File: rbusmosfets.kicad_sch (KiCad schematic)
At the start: 26 parts, among them J1 RBUS, J4 Conn_01x02_Male, Q4 PXP012-30QLJ, Q5 PXP012-30QLJ, Q6 PXP012-30QLJ, Q7 PXP012-30QLJ, U10 LTC4412xS6, U5 74AHC1G00, U6 74AHC1G08, U9 LTC4412xS6

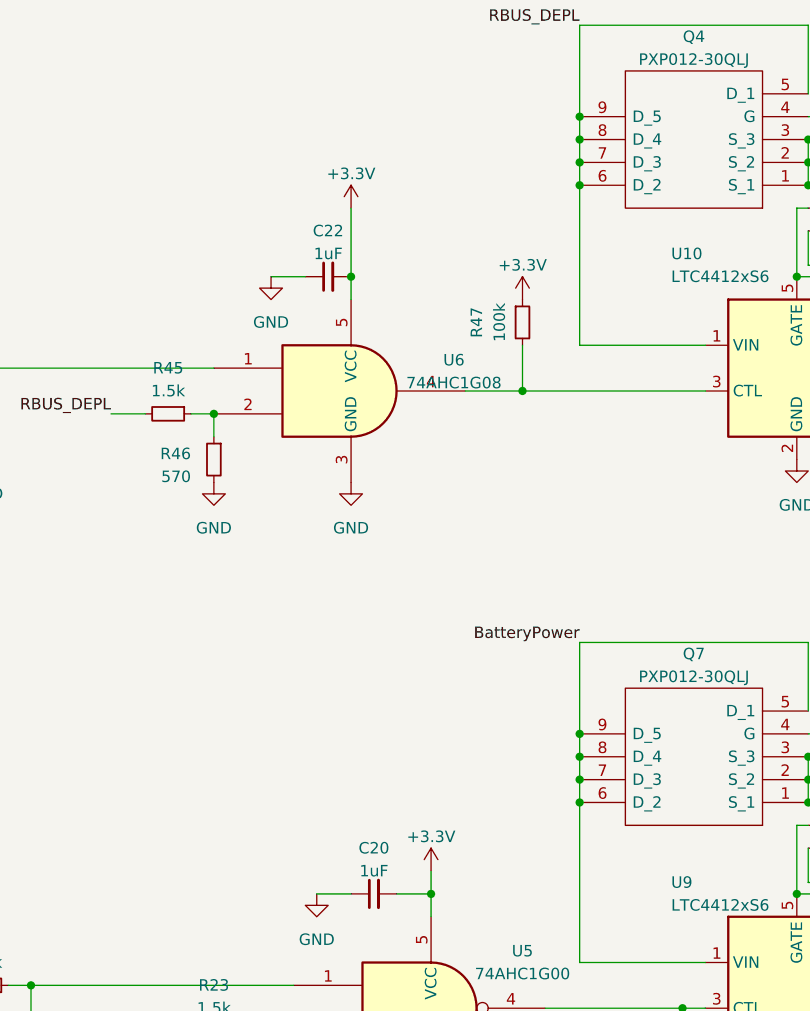
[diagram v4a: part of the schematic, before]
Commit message: almost all drc fixed (65 left)
- J2 hole intersects with pads? USB
- 3.3 regulator courtyard self intersecting?
- courtyard overlaps (does this matter?)
- padstack not valid? this is testpoints on the back with traces on the back, why is this bad?
- expected SMD actual through hole?
- front solder mask bridges items ?? testpoitns are on back layer
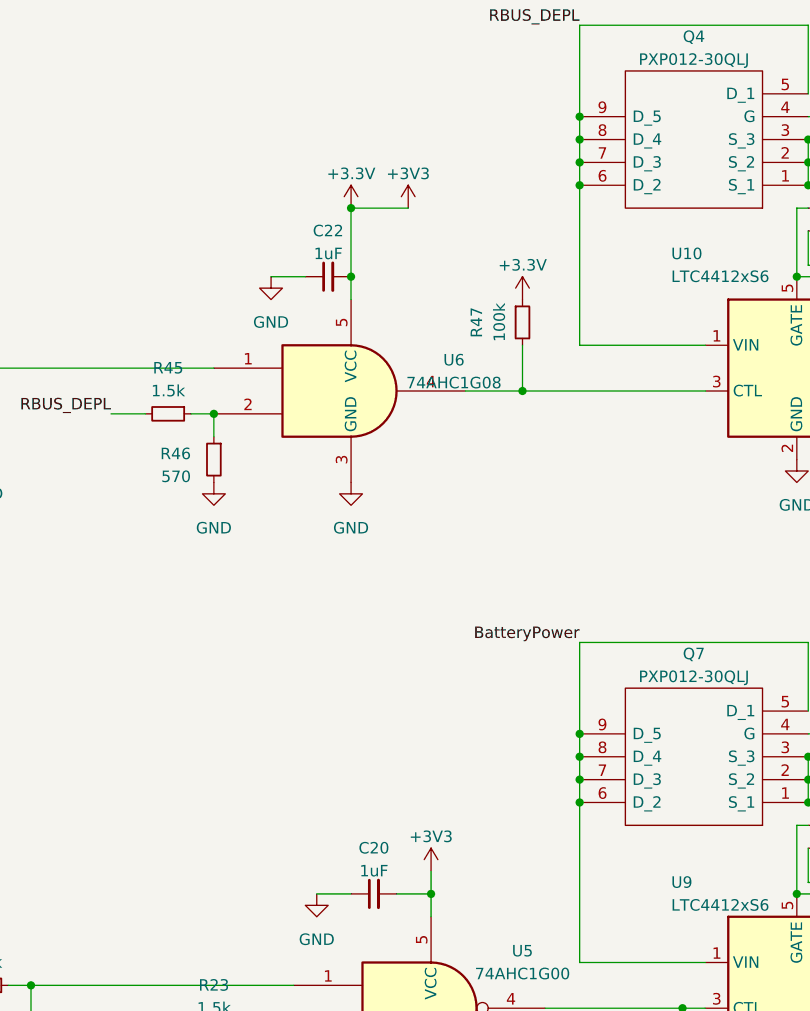
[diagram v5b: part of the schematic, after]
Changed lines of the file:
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@@
   (junction (at 212.09 107.95) (diameter 0) (color 0 0 0 0)
+  )
+  (junction (at 186.69 46.99) (diameter 0) (color 0 0 0 0)
   )
   (junction (at 212.09 110.49) (diameter 0) (color 0 0 0 0)
@@
   )
   (wire (pts (xy 135.89 64.77) (xy 138.43 64.77))
+    (stroke (width 0) (type default))
+  )
+  (wire (pts (xy 186.69 46.99) (xy 193.04 46.99))
     (stroke (width 0) (type default))
   )
@@
     )
   )
+  (symbol (lib_id "power:+3V3") (at 195.58 120.65 0) (unit 1)
+    (in_bom yes) (on_board yes) (dnp no) (fields_autoplaced)
+    (property "Reference" "#PWR083" (at 195.58 124.46 0)
+      (effects (font (size 1.27 1.27)) hide)
+    )
+    (property "Value" "+3V3" (at 195.58 116.84 0)
+      (effects (font (size 1.27 1.27)))
+    )
+    (property "Footprint" "" (at 195.58 120.65 0)
+      (effects (font (size 1.27 1.27)) hide)
+    )
+    (property "Datasheet" "" (at 195.58 120.65 0)
+      (effects (font (size 1.27 1.27)) hide)
+    )
+    (pin "1")
+    (instances
+      (project "Canardboard"
+        (path "/7db990e4-92e1-4f99-b4d2-435bbec1ba83/972bc3cd-df5c-4105-af8a-a8e2a9c5e16b"
+          (reference "#PWR083") (unit 1)
+        )
+      )
+    )
+  )
   (symbol (lib_id "power:VBUS") (at 48.26 59.69 0) (unit 1)
     (in_bom yes) (on_board yes) (dnp no) (fields_autoplaced)
@@
     )
   )
+  (symbol (lib_id "power:+3V3") (at 193.04 46.99 0) (mirror y) (unit 1)
+    (in_bom yes) (on_board yes) (dnp no)
+    (property "Reference" "#PWR051" (at 193.04 50.8 0)
+      (effects (font (size 1.27 1.27)) hide)
+    )
+    (property "Value" "+3V3" (at 193.04 43.18 0)
+      (effects (font (size 1.27 1.27)))
+    )
+    (property "Footprint" "" (at 193.04 46.99 0)
+      (effects (font (size 1.27 1.27)) hide)
+    )
+    (property "Datasheet" "" (at 193.04 46.99 0)
+      (effects (font (size 1.27 1.27)) hide)
+    )
+    (pin "1")
+    (instances
+      (project "Canardboard"
+        (path "/7db990e4-92e1-4f99-b4d2-435bbec1ba83/972bc3cd-df5c-4105-af8a-a8e2a9c5e16b"
+          (reference "#PWR051") (unit 1)
+        )
+      )
+    )
+  )
   (symbol (lib_name "GND_2") (lib_id "power:GND") (at 177.8 54.61 0) (unit 1)
     (in_bom yes) (on_board yes) (dnp no) (fields_autoplaced)
@@
         )
       )
-    )
-  )
-  (symbol (lib_id "power:+3.3V") (at 195.58 120.65 0) (unit 1)
-    (in_bom yes) (on_board yes) (dnp no) (fields_autoplaced)
-    (property "Reference" "#PWR051" (at 195.58 124.46 0)
-      (effects (font (size 1.27 1.27)) hide)
-    )
-    (property "Value" "+3.3V" (at 195.58 116.84 0)
-      (effects (font (size 1.27 1.27)))
-    )
-    (property "Footprint" "" (at 195.58 120.65 0)
-      (effects (font (size 1.27 1.27)) hide)
-    )
-    (property "Datasheet" "" (at 195.58 120.65 0)
-      (effects (font (size 1.27 1.27)) hide)
-    )
-    (pin "1")
-    (instances
-      (project "Canardboard"
-        (path "/7db990e4-92e1-4f99-b4d2-435bbec1ba83/972bc3cd-df5c-4105-af8a-a8e2a9c5e16b"
-          (reference "#PWR051") (unit 1)
-        )
-      )

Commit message: fixed all of andrei's comments v1
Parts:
- removed JP3: SolderJumper_2_Open, Jumper:SolderJumper-2_P1.3mm_Open_RoundedPad1.0x1.5mm, symbol Jumper:SolderJumper_2_Open
- added R48: 100k, Resistor_SMD:R_0402_1005Metric, symbol Device:R_Small
- added R8: 0, Resistor_SMD:R_0402_1005Metric, symbol Device:R_Small
- R15, R42, R44, R46: value 570 -> 470
- R16, R23, R43, R45: value 1.5k -> 1k
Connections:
- net +3.3V: now also R48.1
- net GND: now also R8.2
- net at U5.4, U9.3 (CTL): now also R48.2, R8.1
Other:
- moved on the sheet: C20, R15, R16, R23, R42, U5

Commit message: did some stuffus
added a new power plane in servo power on the back side
made SW larger
and a lot more changes
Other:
- note added: "This is a solder jumper"
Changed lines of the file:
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@@
     (stroke (width 0) (type default))
+  )
+  (text "This is a solder jumper\n" (at 193.04 139.7 0)
+    (effects (font (size 1.27 1.27)) (justify left bottom))
   )
   (label "RBUS_3.3" (at 138.43 173.99 90) (fields_autoplaced)

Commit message: new board just dropped
i hate my life
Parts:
- J4: footprint iclr:AMASS_XT60PW-F -> Connector_AMASS:AMASS_XT30PW-M_1x02_P2.50mm_Horizontal
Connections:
- net BatteryPower: now also J4.2 (Pin_2); no longer J4.1 (Pin_1)
- net GND: now also J4.1 (Pin_1); no longer J4.2 (Pin_2)
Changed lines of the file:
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@@
+    (stroke (width 0) (type default))
+  )
+  (wire (pts (xy 93.98 173.99) (xy 107.95 173.99))
     (stroke (width 0) (type default))
   )
@@
     (stroke (width 0) (type default))
   )
-  (wire (pts (xy 107.95 173.99) (xy 93.98 173.99))
-    (stroke (width 0) (type default))
-  )
   (wire (pts (xy 240.03 26.67) (xy 240.03 36.83))
     (stroke (width 0) (type default))
@@
     (stroke (width 0) (type default))
   )
+  (wire (pts (xy 123.19 171.45) (xy 93.98 171.45))
+    (stroke (width 0) (type default))
+  )
   (wire (pts (xy 163.83 69.85) (xy 160.02 69.85))
     (stroke (width 0) (type default))
@@
   )
   (wire (pts (xy 146.05 64.77) (xy 171.45 64.77))
-    (stroke (width 0) (type default))
-  )
-  (wire (pts (xy 107.95 171.45) (xy 93.98 171.45))
     (stroke (width 0) (type default))
   )
@@
     (effects (font (size 1.27 1.27)) (justify right bottom))
   )
-  (label "BatteryPower" (at 107.95 171.45 0) (fields_autoplaced)
+  (label "BatteryPower" (at 107.95 173.99 0) (fields_autoplaced)
     (effects (font (size 1.27 1.27)) (justify left bottom))
   )
@@
     )
   )
-  (symbol (lib_id "power:GND") (at 107.95 173.99 0) (unit 1)
-    (in_bom yes) (on_board yes) (dnp no)
-    (property "Reference" "#PWR065" (at 107.95 180.34 0)
-      (effects (font (size 1.27 1.27)) hide)
-    )
-    (property "Value" "GND" (at 107.95 179.07 0)
-      (effects (font (size 1.27 1.27)))
-    )
-    (property "Footprint" "" (at 107.95 173.99 0)
-      (effects (font (size 1.27 1.27)) hide)
-    )
-    (property "Datasheet" "" (at 107.95 173.99 0)
-      (effects (font (size 1.27 1.27)) hide)
-    )
-    (pin "1")
-    (instances
-      (project "Canardboard"
-        (path "/7db990e4-92e1-4f99-b4d2-435bbec1ba83/e0402675-af14-46ad-ab53-2a6080ba54c9"
-          (reference "#PWR065") (unit 1)
-        )
-        (path "/7db990e4-92e1-4f99-b4d2-435bbec1ba83/9ac1c7a8-1287-4655-8906-f7f2eef1324f"
-          (reference "#PWR036") (unit 1)
-        )
-        (path "/7db990e4-92e1-4f99-b4d2-435bbec1ba83"
-          (reference "#PWR036") (unit 1)
-        )
-        (path "/7db990e4-92e1-4f99-b4d2-435bbec1ba83/972bc3cd-df5c-4105-af8a-a8e2a9c5e16b"
-          (reference "#PWR036") (unit 1)
-        )
-      )
-    )
-  )
   (symbol (lib_id "Device:R_Small") (at 156.21 143.51 0) (mirror y) (unit 1)
     (in_bom yes) (on_board yes) (dnp no)
@@
       (effects (font (size 1.27 1.27)))
     )
-    (property "Footprint" "iclr:AMASS_XT60PW-F" (at 88.9 171.45 0)
+    (property "Footprint" "Connector_AMASS:AMASS_XT30PW-M_1x02_P2.50mm_Horizontal" (at 88.9 171.45 0)
       (effects (font (size 1.27 1.27)) hide)
     )
@@
         )
       )
+    )
+  )
+  (symbol (lib_id "power:GND") (at 123.19 171.45 0) (unit 1)
+    (in_bom yes) (on_board yes) (dnp no)
+    (property "Reference" "#PWR065" (at 123.19 177.8 0)
+      (effects (font (size 1.27 1.27)) hide)
+    )
+    (property "Value" "GND" (at 123.19 176.53 0)
+      (effects (font (size 1.27 1.27)))
+    )
+    (property "Footprint" "" (at 123.19 171.45 0)
+      (effects (font (size 1.27 1.27)) hide)
+    )
+    (property "Datasheet" "" (at 123.19 171.45 0)
+      (effects (font (size 1.27 1.27)) hide)
+    )
+    (pin "1")
+    (instances
+      (project "Canardboard"
+        (path "/7db990e4-92e1-4f99-b4d2-435bbec1ba83/e0402675-af14-46ad-ab53-2a6080ba54c9"
+          (reference "#PWR065") (unit 1)
+        )
+        (path "/7db990e4-92e1-4f99-b4d2-435bbec1ba83/9ac1c7a8-1287-4655-8906-f7f2eef1324f"
+          (reference "#PWR036") (unit 1)
+        )
+        (path "/7db990e4-92e1-4f99-b4d2-435bbec1ba83"
+          (reference "#PWR036") (unit 1)
+        )
+        (path "/7db990e4-92e1-4f99-b4d2-435bbec1ba83/972bc3cd-df5c-4105-af8a-a8e2a9c5e16b"
+          (reference "#PWR036") (unit 1)
+        )
+      )
